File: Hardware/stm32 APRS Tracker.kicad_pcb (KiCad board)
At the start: 2 copper layers, 83 x 92.5 mm, 127 parts, among them IC1 STM32F103x, P1 USB_B, P101 CONN_01X04, P102 CONN_01X04, P103 CONN_01X01, P2 CONN_01X02, P201 CONN_01X02, P3 CONN_01X01, P301 CONN_01X06, P302 CONN_01X06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

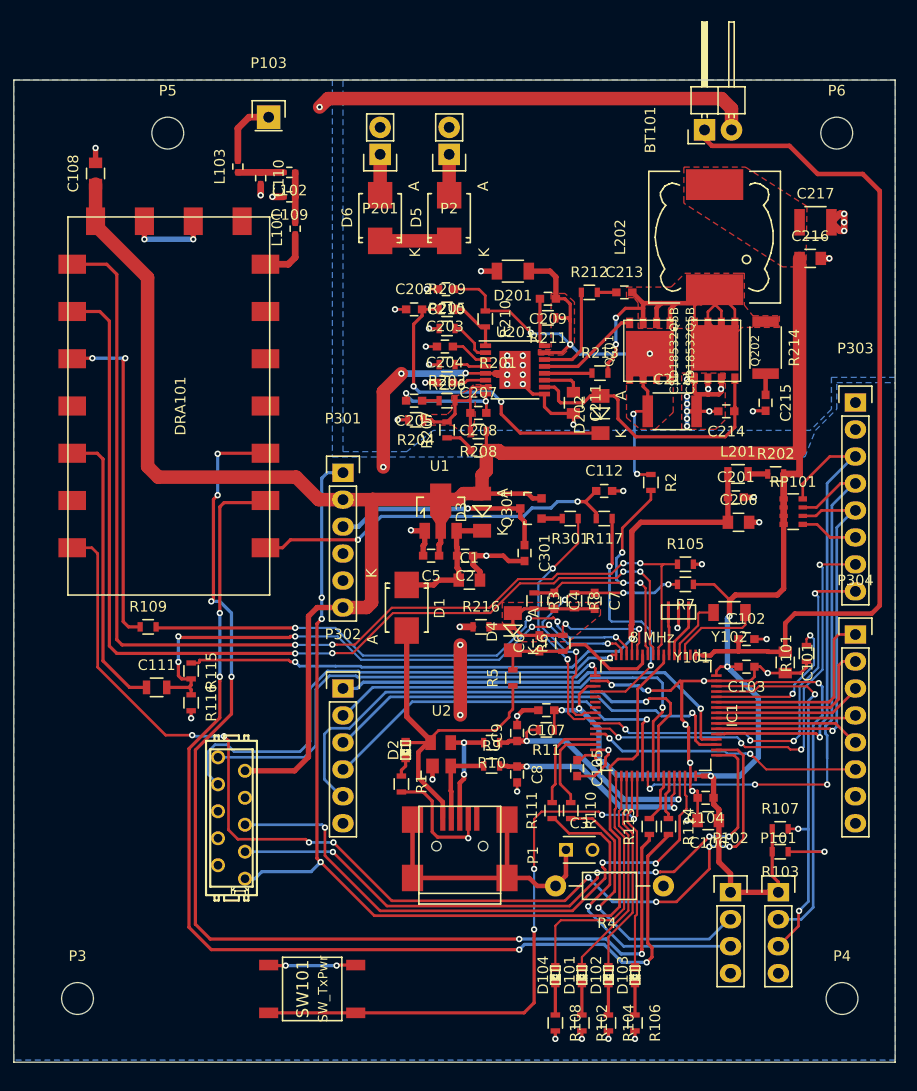
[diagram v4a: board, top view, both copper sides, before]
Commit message: Anpassung des Siebdrucks, USB Buchse rausgeführt
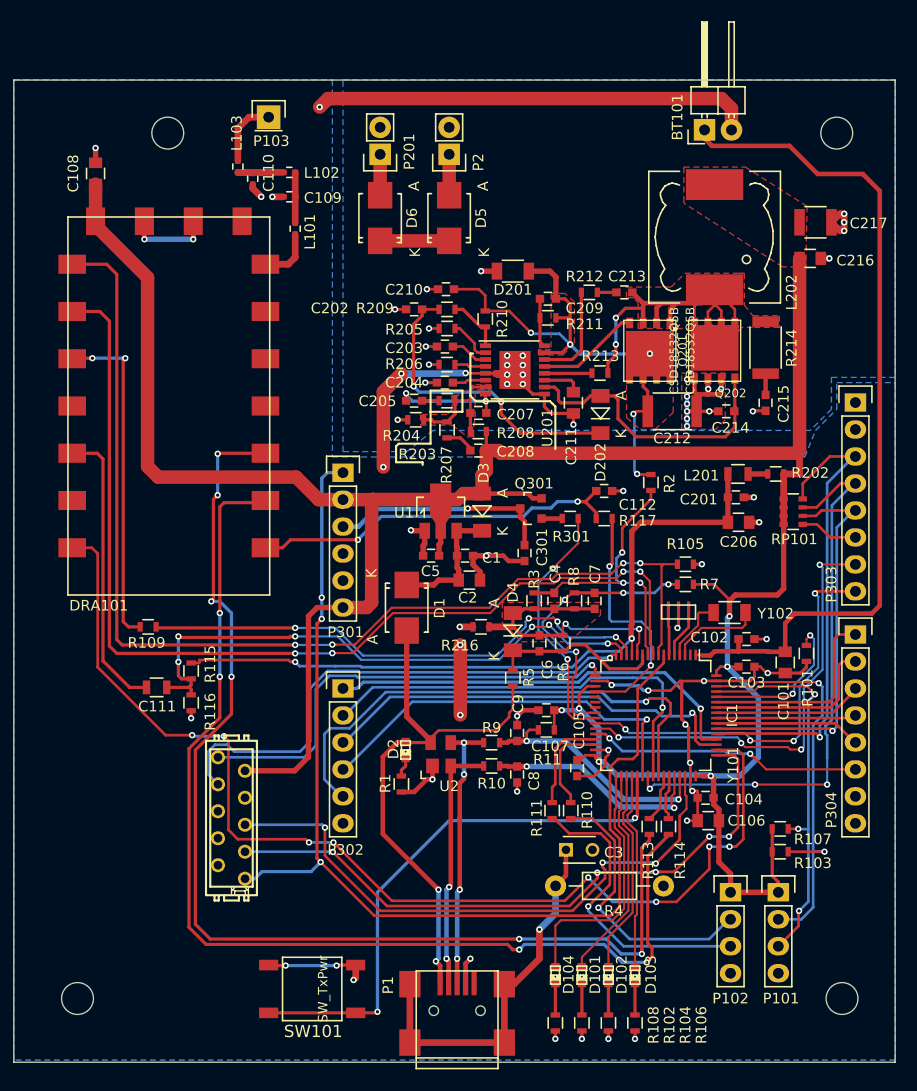
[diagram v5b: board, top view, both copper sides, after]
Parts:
- moved P1 15.5 mm to (107.3, 160.7)
- moved C110 0.75 mm to (88.0, 81.5)
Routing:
- net +5V: track 34.3 -> 52.3 mm, vias 0 -> 2
- net Net-(P1-Pad2): track 8.07 -> 23.8 mm, vias 0 -> 2
- net Net-(P1-Pad3): track 10.4 -> 26.1 mm, vias 2 -> 4
- net Net-(C3-Pad1): track 28.6 -> 35.5 mm, vias 0 -> 1
- net /Tast0: track 56.9 -> 52.7 mm, vias 4 -> 2
- net GND: track 170.2 -> 166.4 mm, vias 38 -> 39
- net Net-(C110-Pad1): track 4.30 -> 5.72 mm
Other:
- board text removed: "KEINE BAUTEILE"
